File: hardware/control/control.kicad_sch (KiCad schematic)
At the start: 25 parts, among them J101 Conn_02x03_Odd_Even, J103 USART, J104 ENCODER, J105 SWITCHES, J106 POSITION, J107 DEBUG, SW102 CENTER_SW

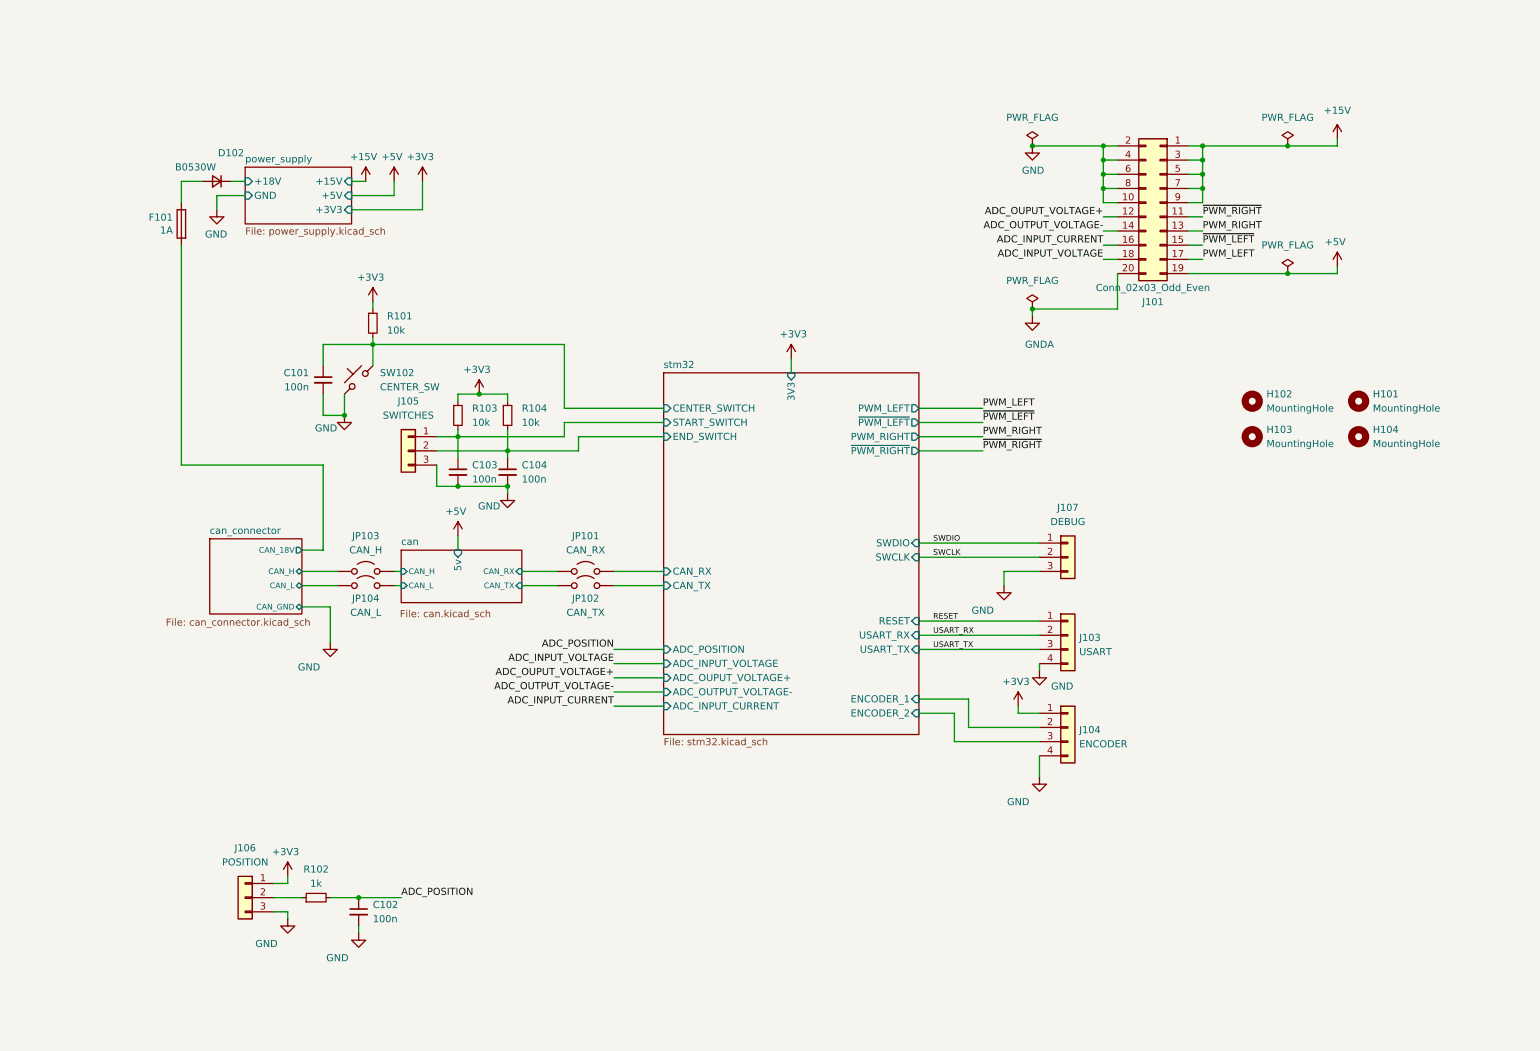
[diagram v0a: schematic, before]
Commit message: Organize schematics per domain
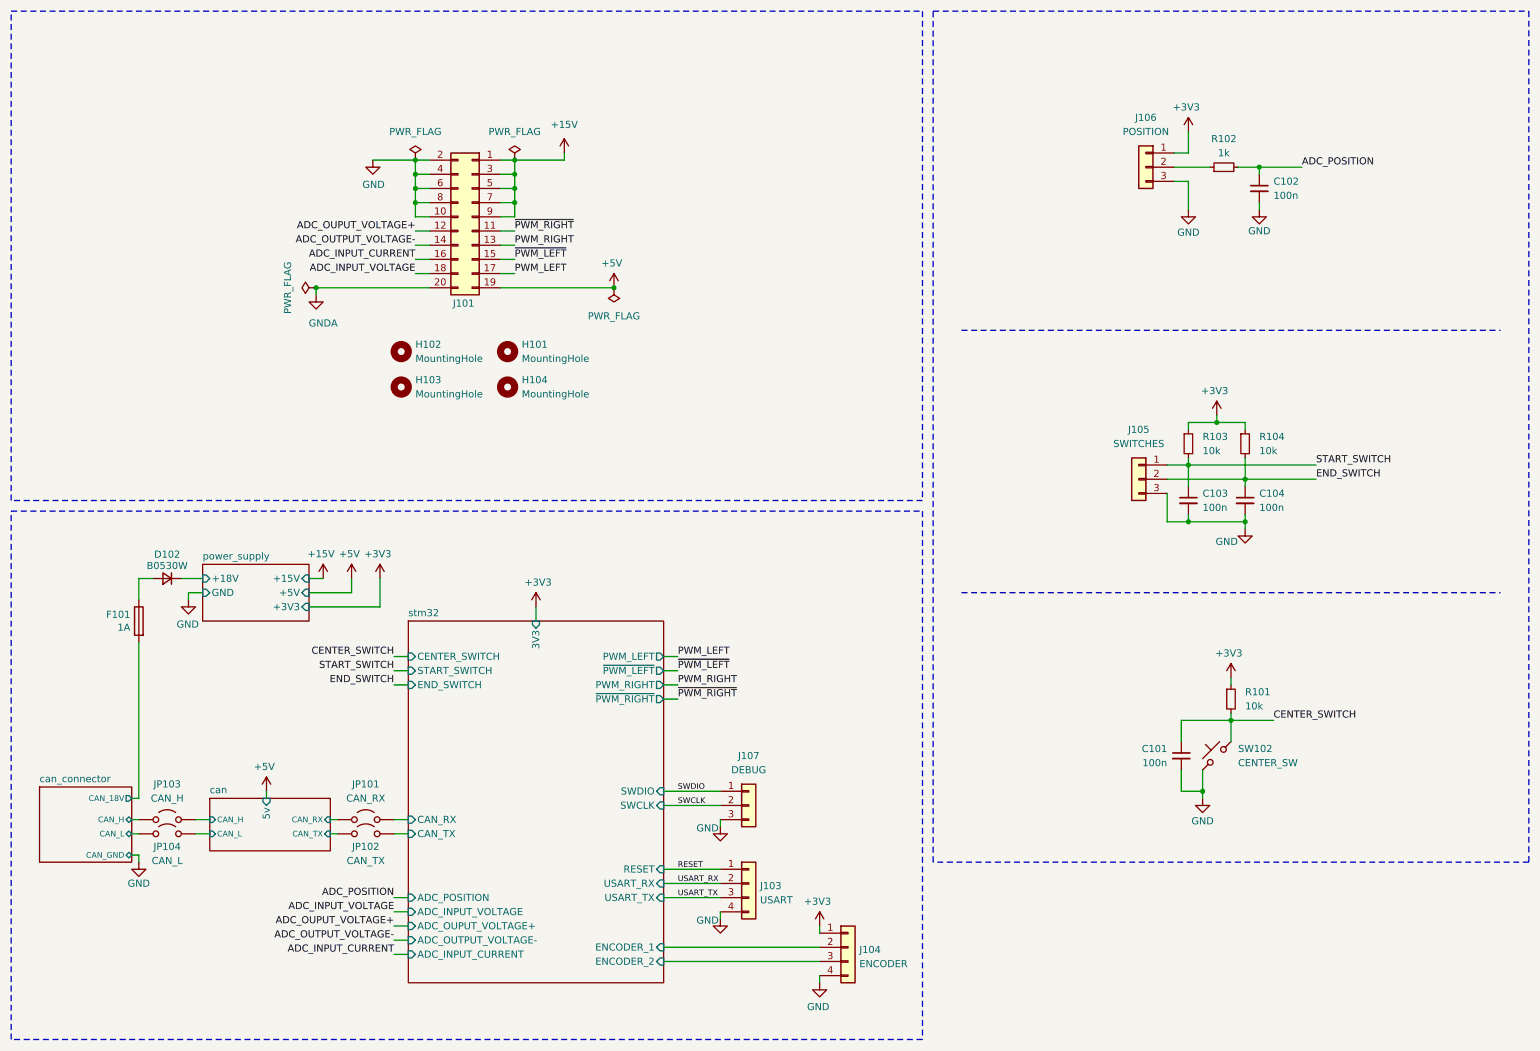
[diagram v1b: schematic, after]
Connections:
- net stm32/CENTER_SWITCH renamed CENTER_SWITCH
- net stm32/END_SWITCH renamed END_SWITCH
- net stm32/START_SWITCH renamed START_SWITCH
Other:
- moved on the sheet: C101, C102, C103, C104, D102, F101, H101, H102, H103, H104, J101, J103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

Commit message: Add schematic hardware plots
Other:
- company: (none) -> Zenite Solar
- title: (none) -> Módulo Direção Eletronica 2025 (MDE25)
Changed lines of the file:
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@@
 	(generator_version "9.0")
 	(paper "A4")
+	(title_block
+		(title "Módulo Direção Eletronica 2025 (MDE25)")
+		(date "2025-07-27")
+		(rev "0.0.1")
+		(company "Zenite Solar")
+		(comment 1 "Placa de Controle")
+	)
 	(rectangle
 		(start 12.7 12.7)
